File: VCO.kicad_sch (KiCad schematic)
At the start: 68 parts, among them K1 SW_SPST, K2 SW_SPST, K3 SW_SPST, P2 100k, P3 100k, P4 4k7, Q3 BC184, Q4 BC183B, Q5 BF244B, Q6 BC184, Q7 BF244B, Q8 BC184, U1 7413, U2 7490, U4 UA747

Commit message: Add missing P1-1-3 connector
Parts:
- added C_Sin1: Conn_01x01, Connector_PinHeader_2.54mm:PinHeader_1x01_P2.54mm_Vertical, symbol Connector_Generic:Conn_01x01
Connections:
- net +5V: now also C_Sin1.1 (Pin_1)
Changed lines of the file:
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@@
   (junction (at 167.64 109.22) (diameter 0) (color 0 0 0 0)
+  )
+  (junction (at 109.22 26.67) (diameter 0) (color 0 0 0 0)
   )
   (junction (at 201.93 101.6) (diameter 0) (color 0 0 0 0)
@@
         )
       )
+    )
+  )
+  (symbol (lib_id "Connector_Generic:Conn_01x01") (at 109.22 31.75 270) (unit 1)
+    (in_bom yes) (on_board yes) (dnp no) (fields_autoplaced)
+    (property "Reference" "C_Sin1" (at 106.68 31.115 90)
+      (effects (font (size 1.27 1.27)) (justify right))
+    )
+    (property "Value" "Conn_01x01" (at 106.68 33.655 90)
+      (effects (font (size 1.27 1.27)) (justify right))
+    )
+    (property "Footprint" "Connector_PinHeader_2.54mm:PinHeader_1x01_P2.54mm_Vertical" (at 109.22 31.75 0)
+      (effects (font (size 1.27 1.27)) hide)
+    )
+    (property "Datasheet" "~" (at 109.22 31.75 0)
+      (effects (font (size 1.27 1.27)) hide)
+    )
+    (pin "1")
+    (instances
+      (project "janel-panel-minimoog"
+        (path "/3cc2a3de-1ac5-4269-8b63-e6b812b486d5/00000000-0000-0000-0000-00005e37b0c8"
+          (reference "C_Sin1") (unit 1)
+        )
+        (path "/3cc2a3de-1ac5-4269-8b63-e6b812b486d5/00000000-0000-0000-0000-00005e12e25c"
+          (reference "P1-1-3") (unit 1)
+        )
+      )

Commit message: Kicad update
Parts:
- renumbered C_Sin1 to K1-1, C_Sin1 to K1-2, C_Sin1 to K2-1, C_Sin1 to K2-2, C_Sin1 to K3-1, C_Sin1 to K3-2, C_Sin1 to P1-1-3, C_Sin1 to P1-2, C_Sin1 to P2-3, C_Sin1 to P3-1, C_Sin1 to P3-3, C_Sin1 to P4-2, C_Sin1 to P4-3

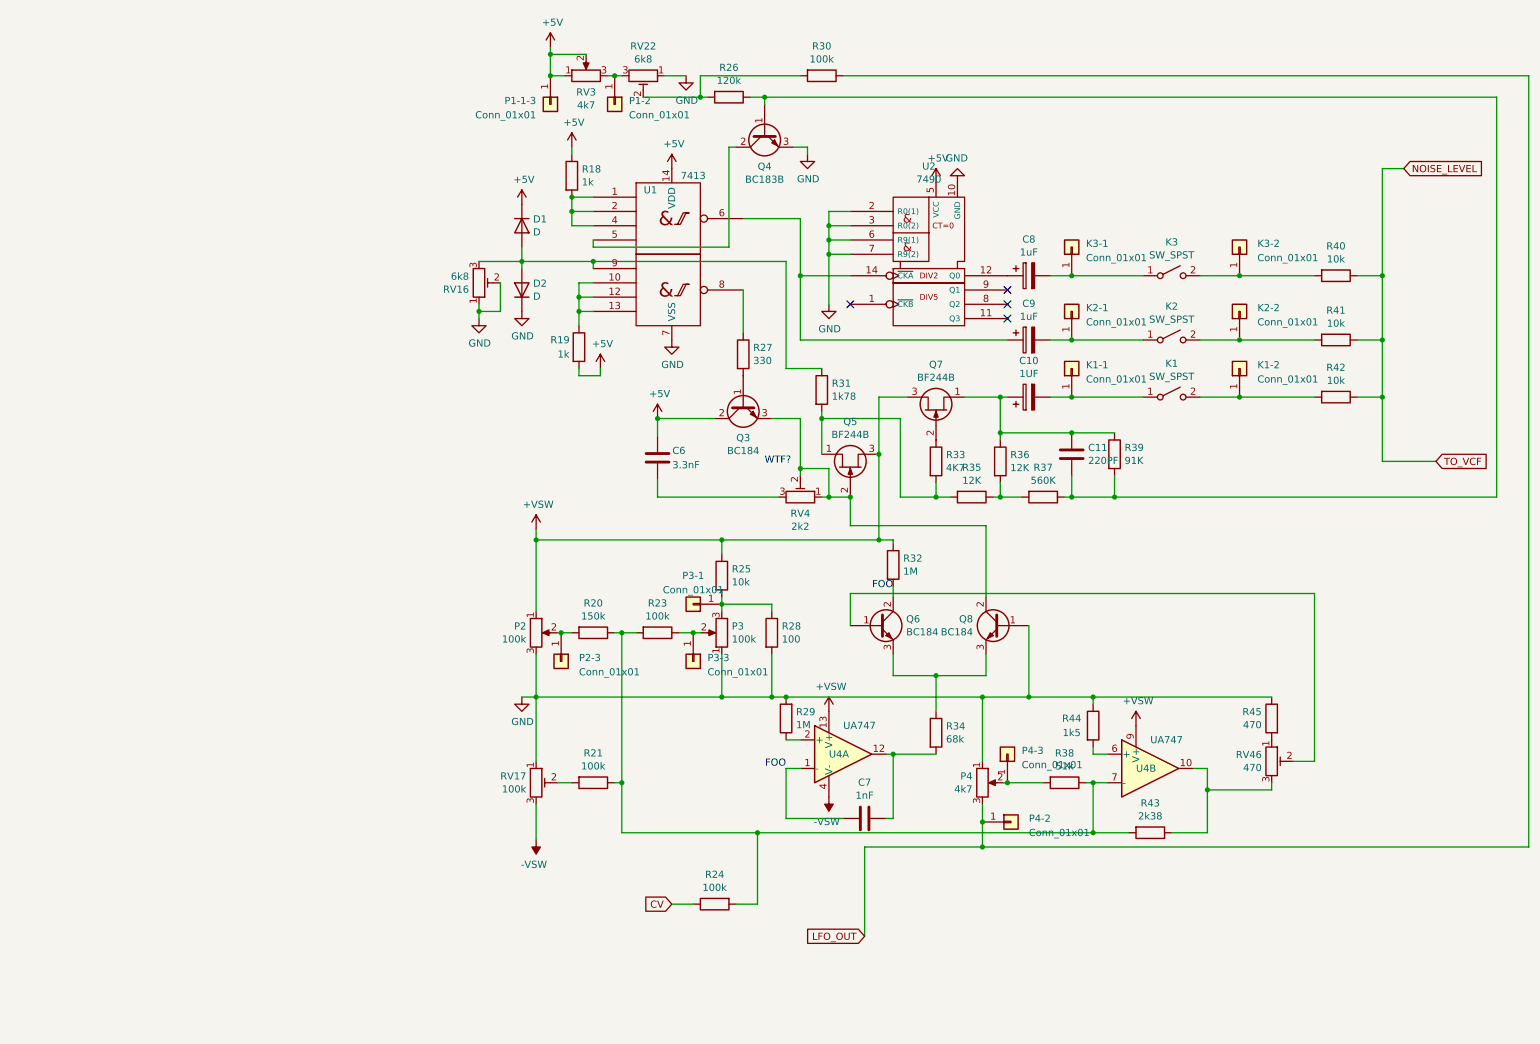
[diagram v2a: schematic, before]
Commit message: Replace symbols with new library
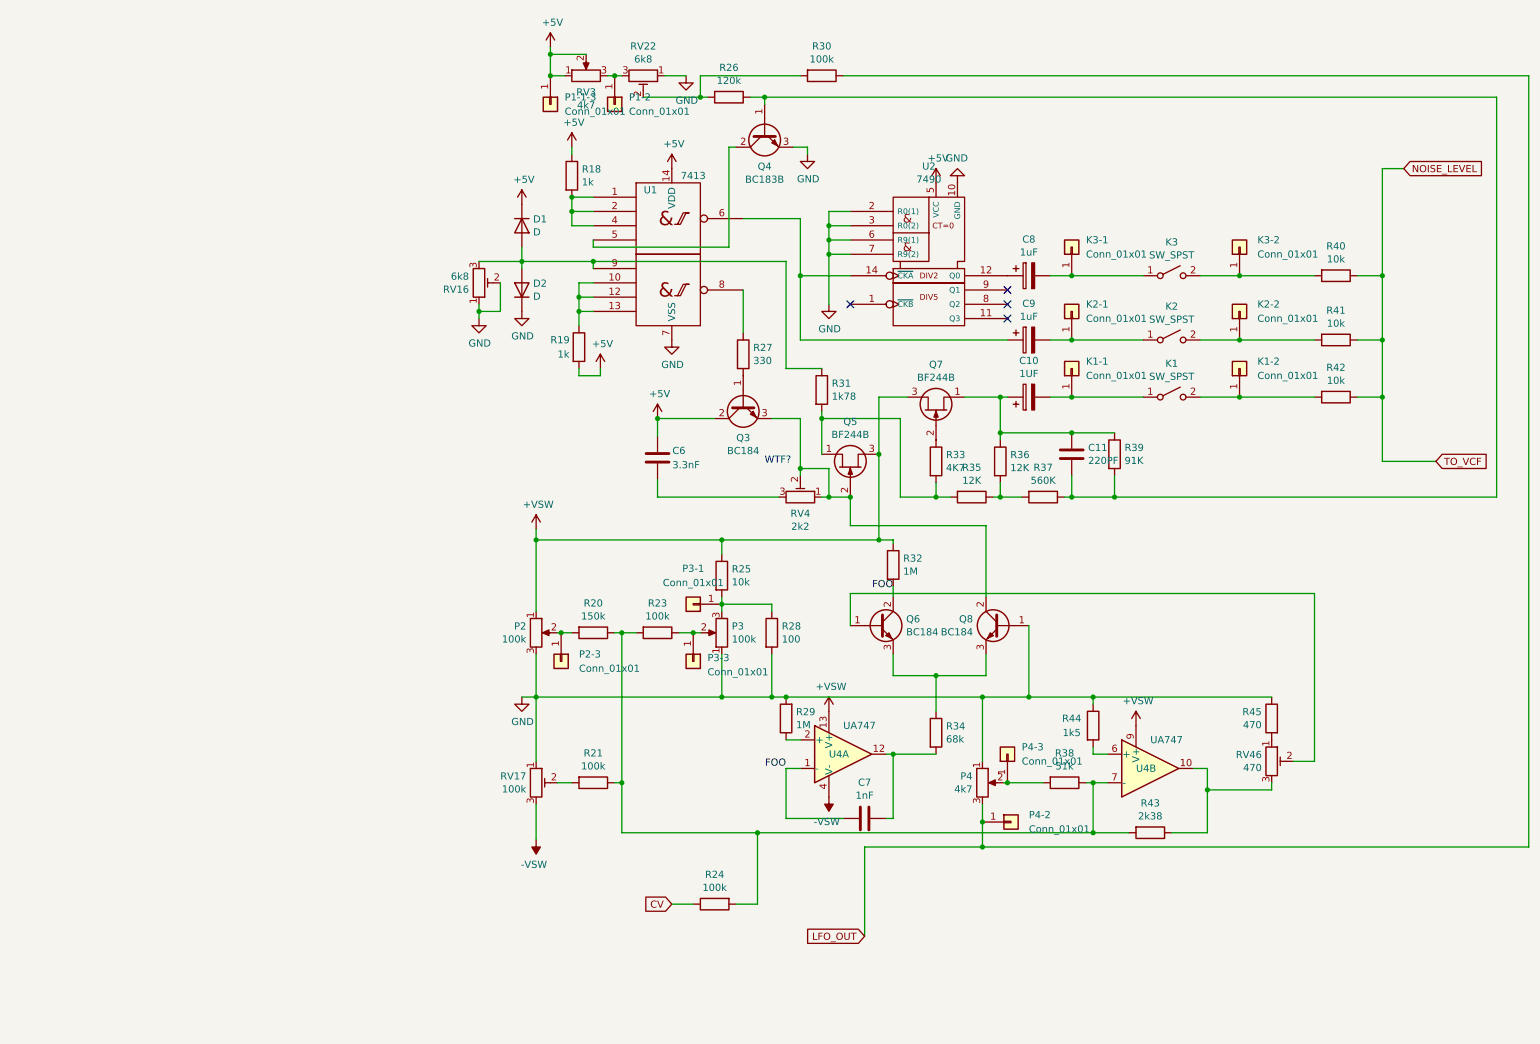
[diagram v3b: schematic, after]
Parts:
- C10, C8: footprint Capacitor_THT:CP_Radial_D6.3mm_P2.50mm -> (none)
- C11, C6, C7: footprint Capacitor_THT:C_Disc_D5.0mm_W2.5mm_P5.00mm -> (none)
- C9: footprint Capacitor_THT:CP_Radial_D8.0mm_P5.00mm -> (none)
- D1, D2: footprint Diode_THT:D_A-405_P10.16mm_Horizontal -> (none)
- K1, K2, K3, P2, P3, P4: footprint Connector_PinSocket_2.54mm:PinSocket_1x03_P2.54mm_Vertical -> (none)
- K1-1, K1-2, K2-1, K2-2, K3-1, K3-2, P1-1-3, P1-2, P2-3, P3-1, P3-3, P4-2, P4-3: footprint Connector_PinHeader_2.54mm:PinHeader_1x01_P2.54mm_Vertical -> (none)
- Q3, Q4, Q6, Q8: symbol Device:Q_NPN_BCE -> Transistor_BJT:Q_NPN_BCE
- Q5, Q7: footprint Package_TO_SOT_THT:TO-92L_Inline_Wide -> Package_TO_SOT_THT:TO-92_Inline
- R18, R19, R20, R21, R23, R24, R25, R26, R27, R28, R29, R30, R31, R32, R33, R34, R35, R36, R37, R38, R39, R40, R41, R42, R43, R44, R45: footprint Resistor_THT:R_Axial_DIN0207_L6.3mm_D2.5mm_P15.24mm_Horizontal -> (none)
- RV16, RV17, RV22, RV3, RV4, RV46: footprint Potentiometer_THT:Potentiometer_Bourns_3296W_Vertical -> (none)
- U4: footprint Package_DIP:DIP-14_W7.62mm_Socket_LongPads -> (none)

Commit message: Replace 7413
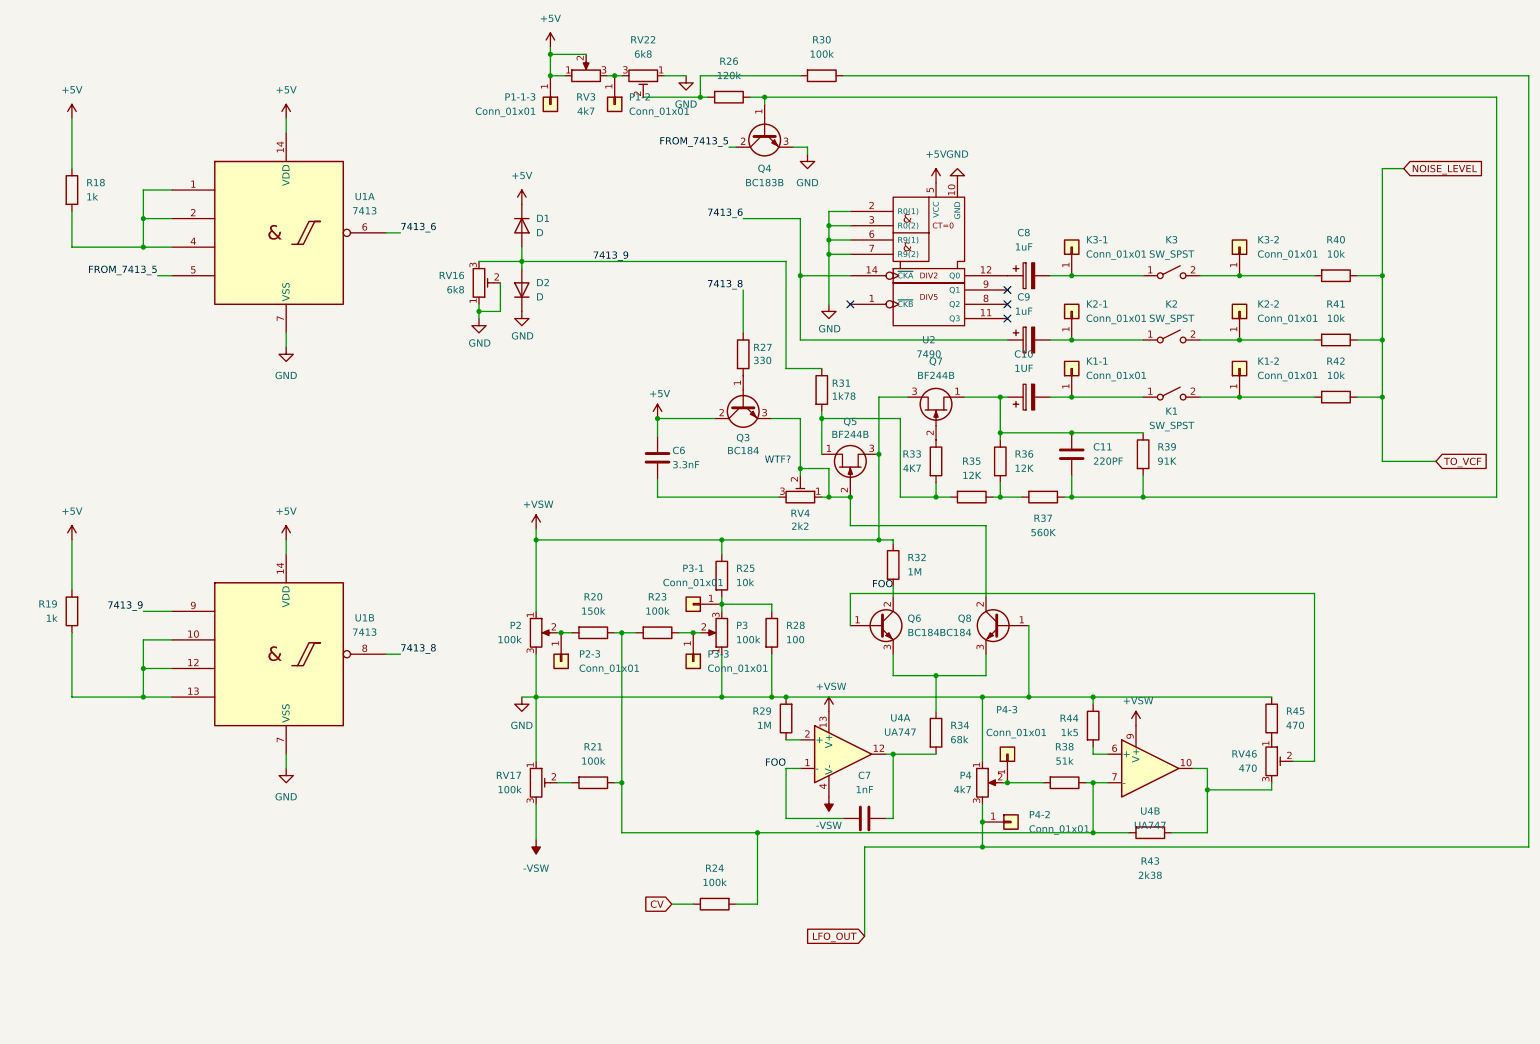
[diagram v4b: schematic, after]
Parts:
- added unit 2 of U1
- U1: footprint Package_DIP:DIP-14_W7.62mm_Socket_LongPads -> (none); symbol janel-panel:7413 -> 74xx_IEEE:7413
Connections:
- net +5V: now also U1.14 (VDD)
- net GND: now also U1.7 (VSS)
- net FROM_7413_5: now reaches Q4.2 (C), U1.5
- net 7413_6: now reaches C9.1, U1.6, U2.14 (~{CKA})
- net 7413_8: now reaches R27.1
- net 7413_8: now also U1.8; no longer U1.8
- net 7413_9: now reaches D1.2 (A), D2.2 (A), R31.1, RV16.3
- net 7413_9: now also U1.9; no longer U1.9
- new net: R19.1, U1.10, U1.12, U1.13
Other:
- moved on the sheet: R18, R19, R39

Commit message: Replace 7490
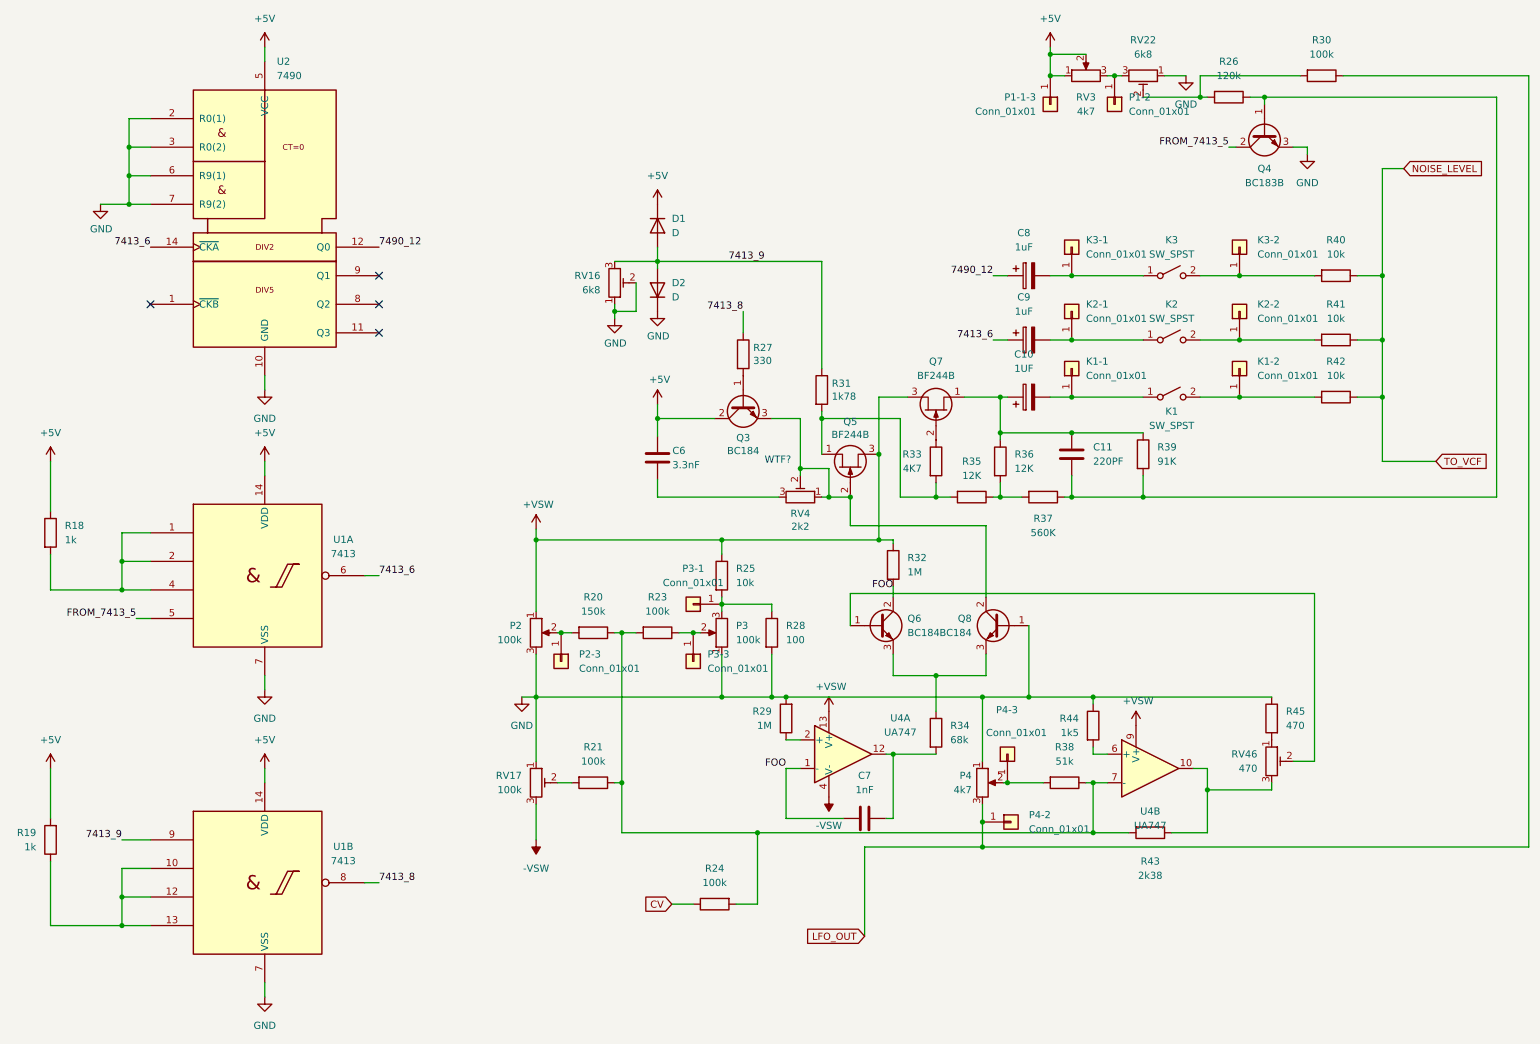
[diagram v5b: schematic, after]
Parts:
- U2: footprint Package_DIP:DIP-14_W7.62mm_Socket_LongPads -> (none); symbol janel-panel:7490 -> 74xx_IEEE:7490
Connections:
- net 7490_12: now reaches C8.1, U2.12 (Q0)
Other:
- moved on the sheet: D1, D2, P1-1-3, P1-2, Q4, R18, R19, R26, R30, RV16, RV22, RV3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
